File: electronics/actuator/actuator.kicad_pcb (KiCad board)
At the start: 2 copper layers, 26 parts, among them J1 Screw_Terminal_01x03, Q1 NTMFS4935NT1G, Q2 NTMFS4935NT1G, Q3 NTMFS4935NT1G, Q4 NTMFS4935NT1G, Q5 NTMFS4935NT1G, Q6 NTMFS4935NT1G, U1 drv8323rs

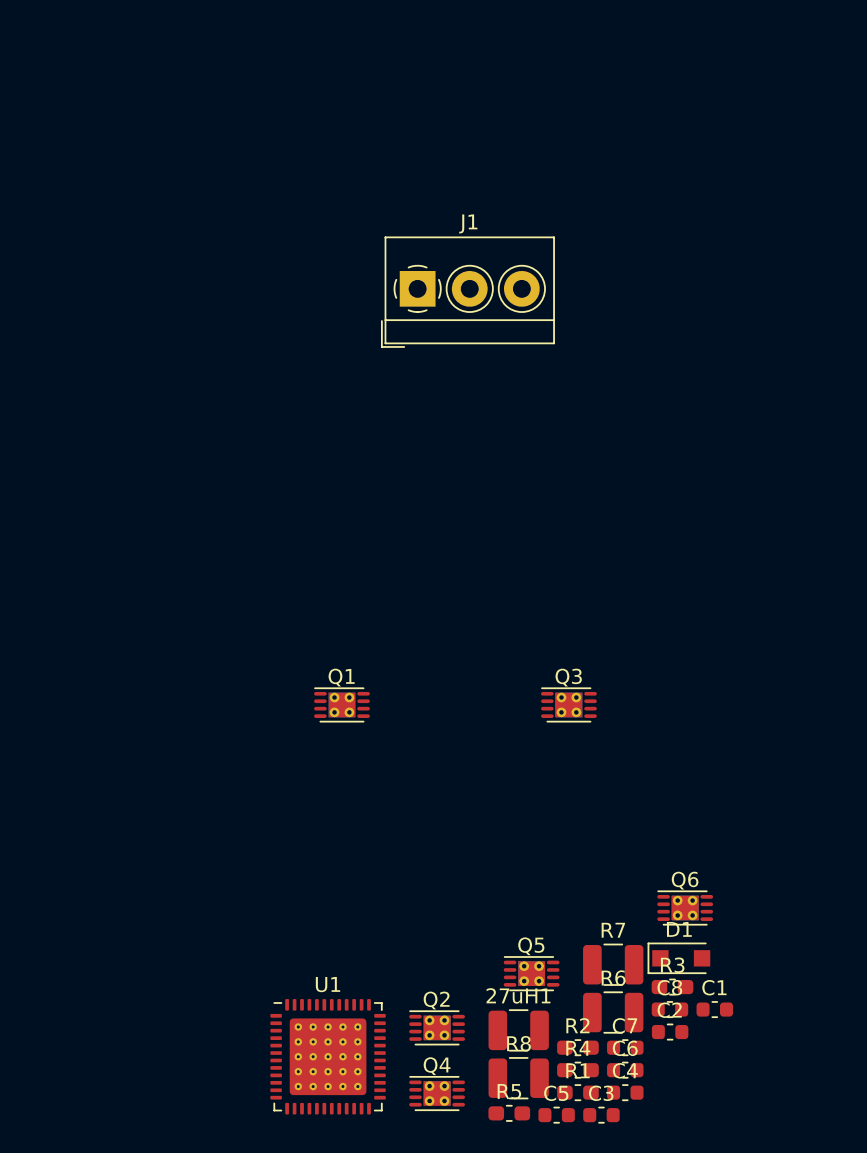
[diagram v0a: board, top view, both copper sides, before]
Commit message: Added SO-FL-8 footprint.
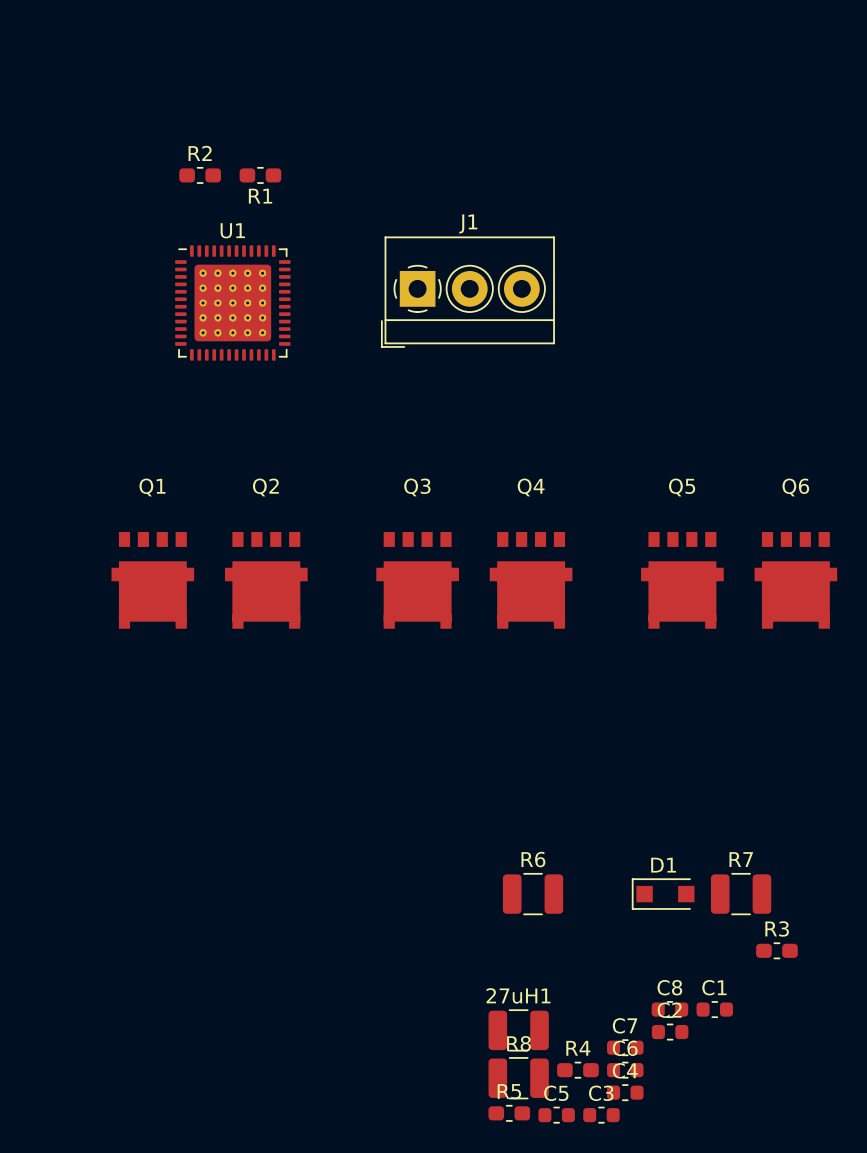
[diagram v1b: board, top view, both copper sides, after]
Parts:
- Q1, Q2, Q3, Q4, Q5, Q6: footprint Package_DFN_QFN:TDFN-8-1EP_3x2mm_P0.5mm_EP1.80x1.65mm_ThermalVias -> actuator:SO-FL-8
- moved R1 65.2 mm to (130.4, 59.7), turned to 180 degrees
- moved R2 63.8 mm to (126.4, 59.7)
- moved U1 51.0 mm to (128.6, 68.3)
- moved Q4 36.3 mm to (148.6, 85.6)
- moved Q2 33.4 mm to (130.8, 85.6)
- moved Q5 29.5 mm to (158.8, 85.6)
- moved Q6 24.4 mm to (166.4, 85.6)
- moved Q1 15.9 mm to (123.2, 85.6)
- moved Q3 14.0 mm to (141.0, 85.6)
- moved R7 9.81 mm to (162.7, 108.0)
- moved R6 9.61 mm to (148.7, 108.0)
- moved R3 7.43 mm to (165.1, 111.8)
- moved D1 4.44 mm to (157.6, 108.0)

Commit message: Added a bunch of stuff and initial layout.
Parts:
- removed C4: 1uF, Capacitor_SMD:C_0603_1608Metric
- added C10: 10uF, Capacitor_SMD:C_0603_1608Metric, F.Cu at (120.6, 61.3)
- added C9: 10uF, Capacitor_SMD:C_0603_1608Metric, F.Cu at (120.6, 58.3)
- added C_DVDD1: 1uF, Capacitor_SMD:C_0603_1608Metric, F.Cu at (141.6, 67.9)
- added C_SW1: 1uF, Capacitor_SMD:C_0603_1608Metric, F.Cu at (131.1, 70.0)
- added C_VCP1: 47uF, Capacitor_SMD:C_0603_1608Metric, F.Cu at (130.3, 67.4)
- added C_VM1: 0.1uF, Capacitor_SMD:C_0603_1608Metric, F.Cu at (128.3, 70.0)
- added J2: PWR_IN, connectors:PhoenixContact_GMSTBA_2,5_2-G-7,62_1x02_P7.62mm_Horizontal, F.Cu at (127.5, 53.2)
- added J3: Pinouts, Connector_PinSocket_2.54mm:PinSocket_1x08_P2.54mm_Vertical, F.Cu at (147.3, 52.3)
- added J4: Pinouts, Connector_PinSocket_2.54mm:PinSocket_1x08_P2.54mm_Vertical, F.Cu at (165.1, 57.9)
- C1: value 0.1uF -> 10uF
- C2: value 47uF -> 10uF
- C3: value 1uF -> 10uF
- J1: value Screw_Terminal_01x03 -> MOTOR_OUT; footprint TerminalBlock_4Ucon:TerminalBlock_4Ucon_1x03_P3.50mm_Horizontal -> connectors:PhoenixContact_GMSTBA_2,5_3-G-7,62_1x03_P7.62mm_Horizontal
- moved C8 62.5 mm to (135.5, 57.3), turned to 270 degrees
- moved 27uH1 61.3 mm to (139.3, 56.4)
- moved C5 61.2 mm to (142.6, 62.0), turned to 90 degrees
- moved C7 59.7 mm to (135.5, 61.8), turned to 90 degrees
- moved R3 56.3 mm to (134.6, 64.5), turned to 180 degrees
- moved C1 52.9 mm to (119.4, 82.9)
- moved R5 50.7 mm to (143.7, 72.1), turned to 180 degrees
- moved D1 50.4 mm to (139.2, 61.0), turned to 180 degrees
- moved R4 46.5 mm to (143.7, 74.0), turned to 180 degrees
- moved C6 44.6 mm to (142.5, 76.9), turned to 180 degrees
- moved C2 40.3 mm to (136.8, 82.9)
- moved C3 40.0 mm to (154.3, 82.8)
- moved R8 39.4 mm to (160.5, 83.0), turned to 180 degrees
- moved J1 35.9 mm to (133.8, 102.5)
- moved R6 34.1 mm to (125.5, 83.0), turned to 180 degrees
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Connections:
- 27uH1 pad 1: VCC -> VAA
- C2 pad 1: Net-(C2-Pad1) -> VDRAIN
- C2 pad 2: Net-(C2-Pad2) -> SNA
- C3 pad 1: Net-(C3-Pad1) -> VDRAIN
- C3 pad 2: VDRAIN -> SNA
- C7 pad 1: VDRAIN -> VCC
- C8 pad 1: VCC -> VAA
- R1 pad 1: VCC -> VAA
- R3 pad 1: VDRAIN -> VCC
- R4 pad 1: VCC -> VAA
- R5 pad 1: VCC -> VAA
- U1 pad 3: Net-(C2-Pad1) -> Net-(C_VCP1-Pad1)
- U1 pad 4: Net-(C2-Pad2) -> Net-(C_VCP1-Pad2)
- U1 pad 47: VDRAIN -> VCC
- U1 pad 5: Net-(C3-Pad1) -> Net-(C_SW1-Pad1)
- U1 pad 6: VDRAIN -> VCC
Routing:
- added copper zone on F.Cu, net SNA
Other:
- board outline added: 52.5 x 55 mm

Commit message: Started routing.
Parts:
- removed 27uH1: L, Inductor_SMD:L_1210_3225Metric
- added L1: 27uH, Inductor_SMD:L_1210_3225Metric, F.Cu at (139.7, 55.9)
- moved C2 9.02 mm to (145.8, 82.8), turned to 180 degrees
- moved Q3 7.50 mm to (145.0, 90.0)
- moved Q4 7.50 mm to (137.5, 87.5)
- moved R7 3.81 mm to (139.2, 82.8), turned to 0 degrees
- moved C6 0.31 mm to (142.5, 77.2)
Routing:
- net GHC: track 0.00 -> 33.9 mm
- net ENABLE: track 0.00 -> 32.3 mm
- net GLC: track 0.00 -> 30.9 mm
- net nSCS: track 0.00 -> 30.2 mm
- net SCLK: track 0.00 -> 29.3 mm
- net nFAULT: track 0.00 -> 28.9 mm
- net SDO: track 0.00 -> 28.6 mm
- net SDI: track 0.00 -> 28.5 mm
- net SOB: track 0.00 -> 27.7 mm
- net SOA: track 0.00 -> 27.6 mm
- net SOC: track 0.00 -> 27.6 mm
- net INHA: track 0.00 -> 27.6 mm
- net GHA: track 0.00 -> 26.9 mm
- net INLA: track 0.00 -> 26.0 mm
- net GHB: track 0.00 -> 25.4 mm
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
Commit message: Still routing...
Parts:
- moved R5 3.05 mm to (146.6, 73.0), turned to 90 degrees
- moved R4 1.12 mm to (144.8, 73.9), turned to 90 degrees
- moved C_VM1 0.38 mm to (127.9, 70.0)
- moved C_SW1 0.38 mm to (130.7, 70.0)
- moved C6 0.26 mm to (142.5, 77.5)
- moved C_VCP1 0.23 mm to (130.2, 67.2)
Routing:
- net DVDD: track 2.41 -> 32.5 mm
- net Net-(R1-Pad2): track 0.00 -> 9.25 mm
- net Net-(C_VCP1-Pad2): track 0.00 -> 5.38 mm
- net INHA: track 27.6 -> 31.5 mm
- net Net-(C_VCP1-Pad1): track 0.00 -> 3.64 mm
- net INLA: track 26.0 -> 29.6 mm
- net GHC: track 33.9 -> 37.2 mm
- net Net-(R3-Pad2): track 0.00 -> 3.01 mm
- net INHB: track 25.2 -> 27.6 mm
- net GHB: track 25.4 -> 27.7 mm
- net ENABLE: track 32.3 -> 34.2 mm
- net GLC: track 30.9 -> 32.6 mm
- net nFAULT: track 28.9 -> 27.5 mm
- net INLB: track 24.3 -> 25.7 mm
- net INLC: track 22.6 -> 21.7 mm
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
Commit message: Still routing.
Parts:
- moved C6 3.72 mm to (142.0, 73.8), turned to 90 degrees
- moved R3 0.90 mm to (133.7, 64.4)
- moved C_VCP1 0.52 mm to (130.1, 66.7)
- moved C_VM1 0.52 mm to (127.8, 69.5)
- moved C_SW1 0.52 mm to (130.6, 69.5)
- moved R6 0.41 mm to (125.1, 83.0)
- moved R8 0.35 mm to (160.1, 83.0)
- moved J1 0.27 mm to (133.7, 102.2)
- moved R7 0.20 mm to (139.2, 83.0)
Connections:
- C10 pad 1: VCC -> VDRAIN
- C6 pad 1: VCC -> VAA
- C7 pad 1: VCC -> VDRAIN
- C9 pad 1: VCC -> VDRAIN
- C_SW1 pad 2: VCC -> VDRAIN
- C_VM1 pad 1: VCC -> VDRAIN
- J2 pad 2: VCC -> VDRAIN
- R3 pad 1: VCC -> VDRAIN
- U1 pad 26: VCC -> VAA
- U1 pad 47: VCC -> VDRAIN
- U1 pad 6: VCC -> VDRAIN
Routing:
- net SNA: track 0.00 -> 58.9 mm, vias 0 -> 6
- net C_OUT: track 0.00 -> 37.4 mm
- net SPC: track 0.00 -> 30.0 mm
- net A_OUT: track 0.00 -> 24.8 mm
- net VDRAIN: track 0.00 -> 23.2 mm
- net B_OUT: track 0.00 -> 18.8 mm
- net Net-(C5-Pad2): track 0.00 -> 17.9 mm
- net SPA: track 0.00 -> 14.7 mm
- net SPB: track 0.00 -> 10.3 mm, vias 0 -> 2
- net Net-(C_SW1-Pad1): track 0.00 -> 3.06 mm
- net GHA: track 27.1 -> 28.8 mm
- net SOA: track 28.0 -> 28.8 mm
- net Net-(C_VCP1-Pad2): track 5.38 -> 6.01 mm
- added copper zone on F.Cu, net A_OUT
- added copper zone on F.Cu, net B_OUT
- added copper zone on F.Cu, net C_OUT
- added copper zone on F.Cu, net SPA
- added copper zone on F.Cu, net SPB
- added copper zone on F.Cu, net SPC
- removed copper zone on F.Cu, net SNA

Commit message: Finished pcb.
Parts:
- moved C5 0.83 mm to (142.6, 61.2)
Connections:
- U1 pad 49: (no net) -> SNA
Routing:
- net VAA: track 0.00 -> 43.7 mm, vias 0 -> 3
- net B_OUT: track 18.8 -> 15.5 mm
- net A_OUT: track 24.8 -> 21.8 mm
- net C_OUT: track 37.4 -> 34.5 mm
- net SNA: track 58.9 -> 59.7 mm, vias 6 -> 28
- net Net-(C5-Pad2): track 17.9 -> 17.2 mm
- net VDRAIN: vias 0 -> 9
- added copper zone on B.Cu, net SNA
- added copper zone on F.Cu, net SNA
- added copper zone on B.Cu, net VDRAIN
- added copper zone on F.Cu, net VDRAIN
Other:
- net class Default: clearance 0.2 -> 0.15
- rule trace_clearance: 0.2 -> 0.15

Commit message: Finished board.
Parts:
- U1: footprint Package_DFN_QFN:Texas_S-PVQFN-N48_EP5.15x5.15mm_ThermalVias -> actuator:Texas_S-PVQFN-N48_EP5.15x5.15mm_ThermalVias
- moved C_VCP1 0.79 mm to (129.3, 66.7)
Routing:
- net SNA: track 59.7 -> 61.8 mm
- net Net-(C_VCP1-Pad1): track 4.13 -> 4.74 mm
- net Net-(C_VCP1-Pad2): track 6.01 -> 6.58 mm
